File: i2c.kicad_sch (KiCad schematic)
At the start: 2 parts, among them U1 74HC237, U2 74HC237

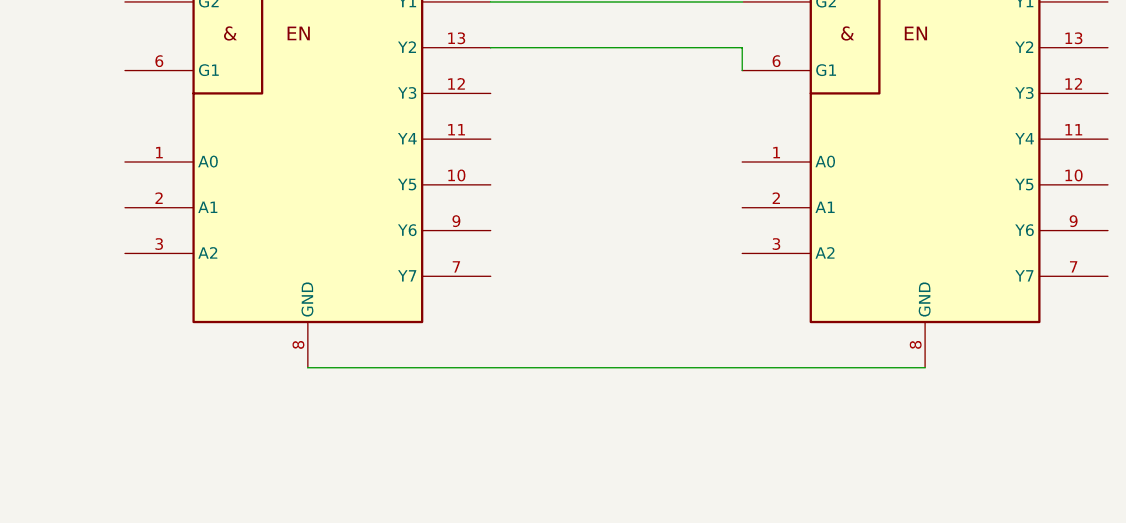
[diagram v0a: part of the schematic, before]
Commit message: se agregaron nuevas lineas de comunicacion
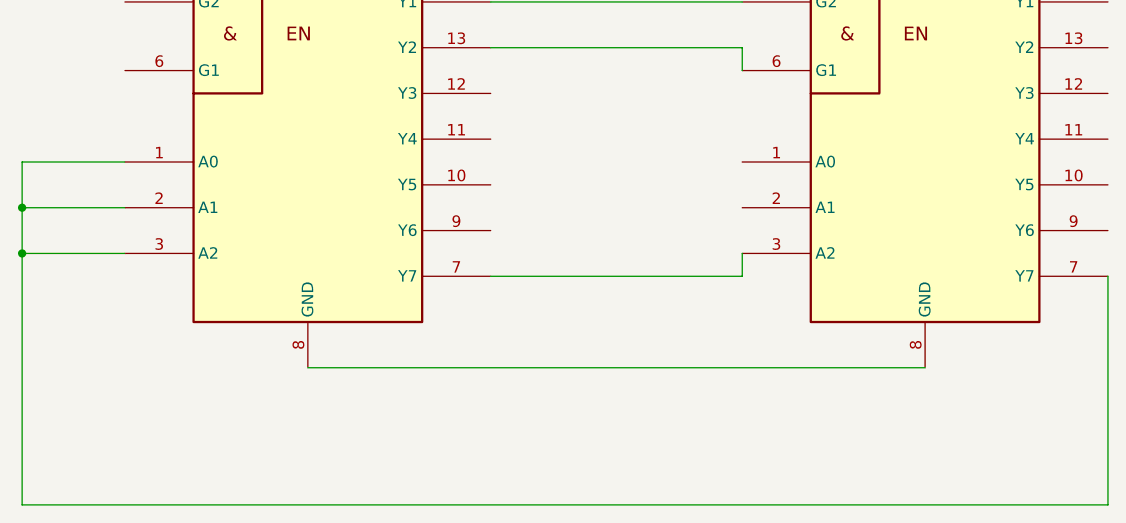
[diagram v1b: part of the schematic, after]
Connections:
- net at U2.3 (A2): now also U1.7 (Y7)
- net at U2.7 (Y7): now also U1.1 (A0), U1.2 (A1), U1.3 (A2)
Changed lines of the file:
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@@
 	(generator_version "9.0")
 	(paper "A4")
+	(junction
+		(at 53.34 71.12)
+		(diameter 0)
+		(color 0 0 0 0)
+	)
+	(junction
+		(at 53.34 76.2)
+		(diameter 0)
+		(color 0 0 0 0)
+	)
+	(wire
+		(pts
+			(xy 53.34 76.2) (xy 53.34 71.12)
+		)
+		(stroke
+			(width 0)
+			(type default)
+		)
+	)
 	(wire
 		(pts
 			(xy 105.41 53.34) (xy 133.35 53.34)
+		)
+		(stroke
+			(width 0)
+			(type default)
+		)
+	)
+	(wire
+		(pts
+			(xy 53.34 66.04) (xy 64.77 66.04)
+		)
+		(stroke
+			(width 0)
+			(type default)
+		)
+	)
+	(wire
+		(pts
+			(xy 133.35 78.74) (xy 133.35 76.2)
+		)
+		(stroke
+			(width 0)
+			(type default)
+		)
+	)
+	(wire
+		(pts
+			(xy 173.99 78.74) (xy 173.99 104.14)
 		)
 		(stroke
@@
 	(wire
 		(pts
+			(xy 105.41 78.74) (xy 133.35 78.74)
+		)
+		(stroke
+			(width 0)
+			(type default)
+		)
+	)
+	(wire
+		(pts
+			(xy 173.99 104.14) (xy 53.34 104.14)
+		)
+		(stroke
+			(width 0)
+			(type default)
+		)
+	)
+	(wire
+		(pts
 			(xy 105.41 48.26) (xy 133.35 48.26)
 		)
 		(stroke
+			(width 0)
+			(type default)
+		)
+	)
+	(wire
+		(pts
+			(xy 53.34 76.2) (xy 64.77 76.2)
+		)
+		(stroke
+			(width 0)
+			(type default)
+		)
+	)
+	(wire
+		(pts
+			(xy 53.34 71.12) (xy 53.34 66.04)
+		)
+		(stroke
+			(width 0)
+			(type default)
+		)
+	)
+	(wire
+		(pts
+			(xy 53.34 104.14) (xy 53.34 76.2)
+		)
+		(stroke
+			(width 0)
+			(type default)
+		)
+	)
+	(wire
+		(pts
+			(xy 53.34 71.12) (xy 64.77 71.12)
+		)
+		(stroke

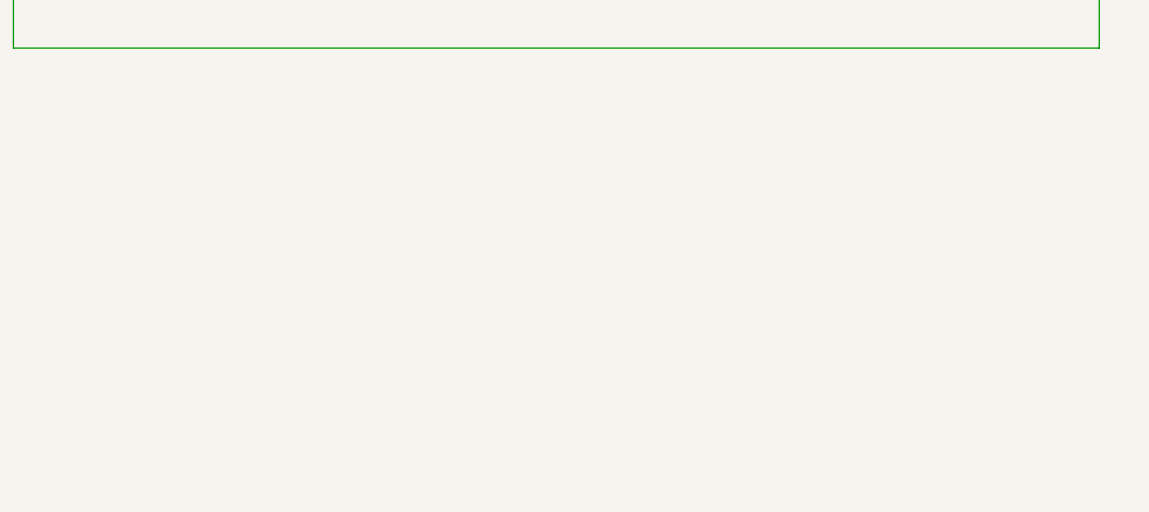
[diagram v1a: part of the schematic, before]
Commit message: se agregaron 2 componentes nuevos
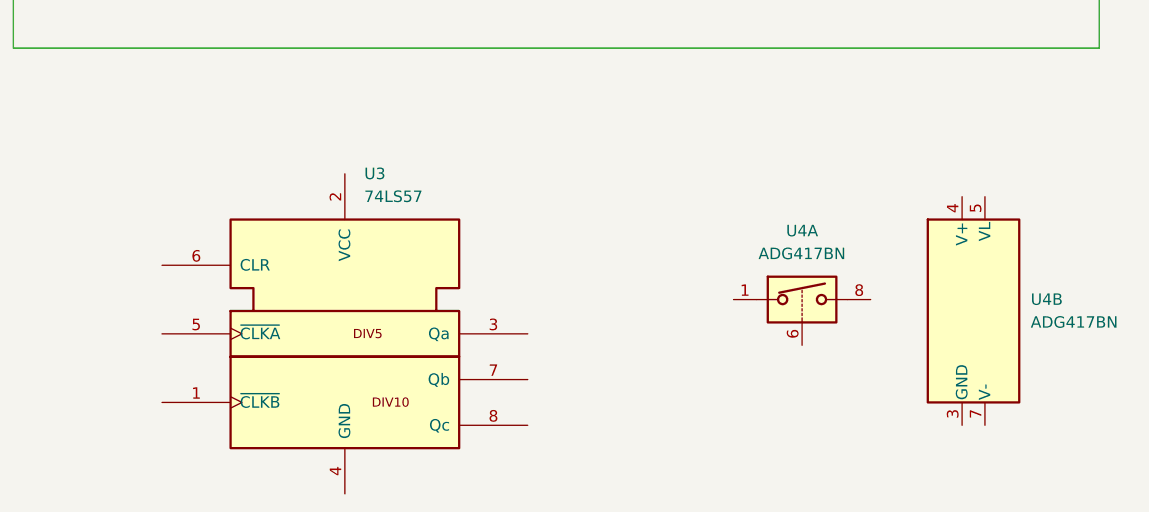
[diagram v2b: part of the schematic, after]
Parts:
- added U3: 74LS57, symbol 74xx_IEEE:74LS57
- added U4: ADG417BN, Package_DIP:DIP-8_W7.62mm, symbol Analog_Switch:ADG417BN
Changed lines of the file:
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@@
+	)
+	(symbol
+		(lib_id "Analog_Switch:ADG417BN")
+		(at 158.75 133.35 0)
+		(unit 2)
+		(exclude_from_sim no)
+		(in_bom yes)
+		(on_board yes)
+		(dnp no)
+		(fields_autoplaced yes)
+		(property "Reference" "U4"
+			(at 166.37 132.0799 0)
+			(effects
+				(font
+					(size 1.27 1.27)
+				)
+				(justify left)
+			)
+		)
+		(property "Value" "ADG417BN"
+			(at 166.37 134.6199 0)
+			(effects
+				(font
+					(size 1.27 1.27)
+				)
+				(justify left)
+			)
+		)
+		(property "Footprint" "Package_DIP:DIP-8_W7.62mm"
+			(at 158.75 135.89 0)
+			(effects
+				(font
+					(size 1.27 1.27)
+				)
+				(hide yes)
+			)
+		)
+		(property "Datasheet" "https://www.analog.com/media/en/technical-documentation/data-sheets/ADG417.pdf"
+			(at 158.75 133.35 0)
+			(effects
+				(font
+					(size 1.27 1.27)
+				)
+				(hide yes)
+			)
+		)
+		(property "Description" "Single SPST Monolithic LC²MOS Analog Switch, normally OFF, 25Ohm Ron, DIP-8"
+			(at 158.75 133.35 0)
+			(effects
+				(font
+					(size 1.27 1.27)
+				)
+				(hide yes)
+			)
+		)
+		(pin "5"
+		)
+		(pin "2"
+		)
+		(pin "3"
+		)
+		(pin "6"
+		)
+		(pin "8"
+		)
+		(pin "1"
+		)
+		(pin "4"
+		)
+		(pin "7"
+		)
+		(instances
+			(project ""
+				(path "/5d2edb2c-ac7e-435f-ae04-6809c3a8fc26"
+					(reference "U4")
+					(unit 2)
+				)
+			)
+		)
+	)
+	(symbol
+		(lib_id "Analog_Switch:ADG417BN")
+		(at 140.97 132.08 0)
+		(unit 1)
+		(exclude_from_sim no)
+		(in_bom yes)
+		(on_board yes)
+		(dnp no)
+		(fields_autoplaced yes)
+		(property "Reference" "U4"
+			(at 140.97 124.46 0)
+			(effects
+				(font
+					(size 1.27 1.27)
+				)
+			)
+		)
+		(property "Value" "ADG417BN"
+			(at 140.97 127 0)
+			(effects
+				(font
+					(size 1.27 1.27)
+				)
+			)
+		)
+		(property "Footprint" "Package_DIP:DIP-8_W7.62mm"
+			(at 140.97 134.62 0)
+			(effects
+				(font
+					(size 1.27 1.27)
+				)
+				(hide yes)
+			)
+		)
+		(property "Datasheet" "https://www.analog.com/media/en/technical-documentation/data-sheets/ADG417.pdf"
+			(at 140.97 132.08 0)
+			(effects
+				(font
+					(size 1.27 1.27)
+				)
+				(hide yes)
+			)
+		)
+		(property "Description" "Single SPST Monolithic LC²MOS Analog Switch, normally OFF, 25Ohm Ron, DIP-8"
+			(at 140.97 132.08 0)
+			(effects
+				(font
+					(size 1.27 1.27)
+				)
+				(hide yes)
+			)
+		)
+		(pin "5"
+		)
+		(pin "2"
+		)
+		(pin "3"
+		)
+		(pin "6"
+		)
+		(pin "8"
+		)
+		(pin "1"
+		)
+		(pin "4"
+		)
+		(pin "7"
+		)
+		(instances
+			(project ""
+				(path "/5d2edb2c-ac7e-435f-ae04-6809c3a8fc26"
+					(reference "U4")
+					(unit 1)
+				)
+			)
+		)
+	)
+	(symbol
+		(lib_id "74xx_IEEE:74LS57")
+		(at 90.17 135.89 0)
+		(unit 1)
+		(exclude_from_sim no)
+		(in_bom yes)
+		(on_board yes)
+		(dnp no)
+		(fields_autoplaced yes)
+		(property "Reference" "U3"
+			(at 92.3133 118.11 0)
+			(effects
+				(font
+					(size 1.27 1.27)
+				)
+				(justify left)
+			)
+		)
+		(property "Value" "74LS57"
+			(at 92.3133 120.65 0)
+			(effects
+				(font
+					(size 1.27 1.27)
+				)
+				(justify left)
+			)
+		)
+		(property "Footprint" ""
+			(at 90.17 135.89 0)
+			(effects
+				(font
+					(size 1.27 1.27)
+				)
+				(hide yes)
+			)
+		)
+		(property "Datasheet" ""
+			(at 90.17 135.89 0)
+			(effects
+				(font
+					(size 1.27 1.27)
+				)
+				(hide yes)
+			)
+		)
+		(property "Description" ""
+			(at 90.17 135.89 0)
+			(effects
+				(font
+					(size 1.27 1.27)
+				)
+				(hide yes)
+			)
+		)
+		(pin "2"
+		)
+		(pin "6"
+		)
+		(pin "3"
+		)
+		(pin "7"
+		)
+		(pin "5"
+		)
+		(pin "1"
+		)
+		(pin "8"
+		)
+		(pin "4"
+		)
+		(instances
+			(project ""
+				(path "/5d2edb2c-ac7e-435f-ae04-6809c3a8fc26"
+					(reference "U3")
+					(unit 1)
+				)
+			)
+		)
 	)
 	(symbol

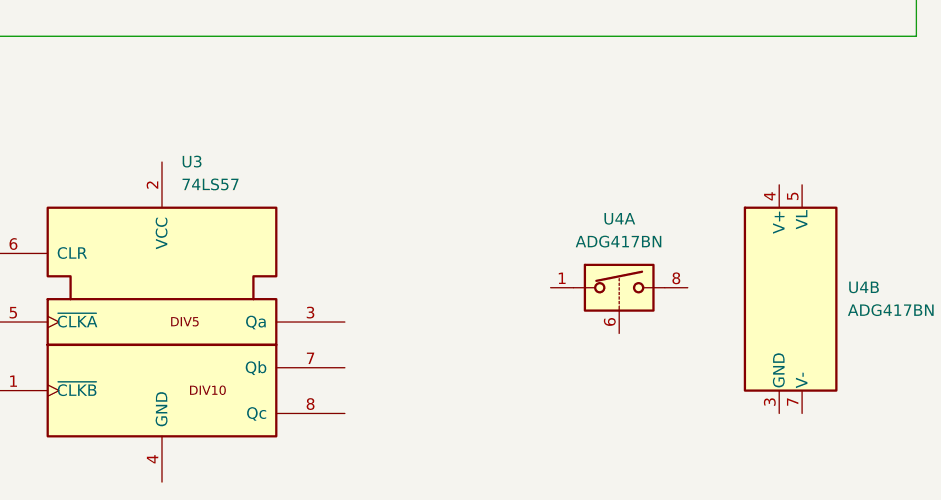
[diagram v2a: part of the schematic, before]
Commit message: se agregaron 2 componenetes nuevos y se ajusto el pcb, falta agregar footprints
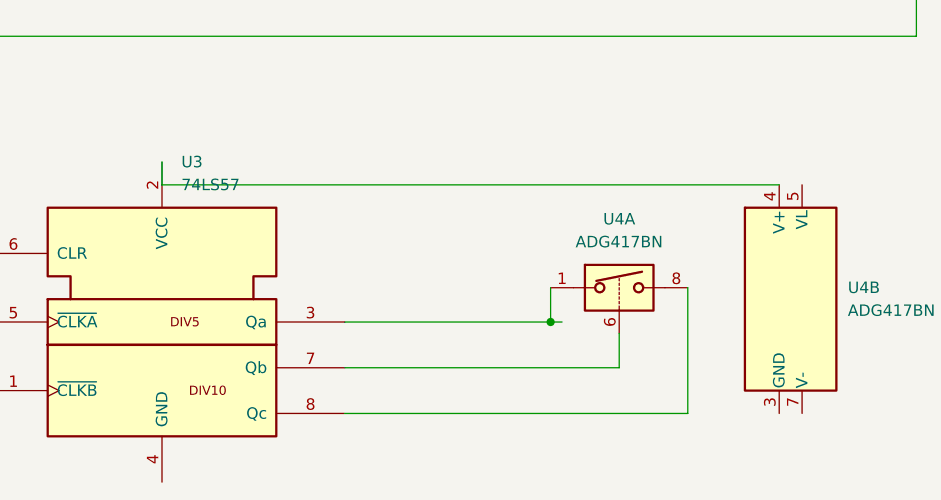
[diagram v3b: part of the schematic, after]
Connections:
- net at U4.4 (V+): now also U3.2 (VCC)
- net at U4.1: now also U3.3 (Qa)
- net at U4.6: now also U3.7 (Qb)
- net at U4.8: now also U3.8 (Qc)
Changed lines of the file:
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@@
+		(color 0 0 0 0)
+	)
+	(junction
+		(at 133.35 135.89)
+		(diameter 0)
 		(color 0 0 0 0)
 	)
@@
 	(wire
 		(pts
+			(xy 133.35 135.89) (xy 133.35 132.08)
+		)
+		(stroke
+			(width 0)
+			(type default)
+		)
+	)
+	(wire
+		(pts
+			(xy 140.97 140.97) (xy 140.97 137.16)
+		)
+		(stroke
+			(width 0)
+			(type default)
+		)
+	)
+	(wire
+		(pts
+			(xy 110.49 146.05) (xy 148.59 146.05)
+		)
+		(stroke
+			(width 0)
+			(type default)
+		)
+	)
+	(wire
+		(pts
+			(xy 158.75 120.65) (xy 90.17 120.65)
+		)
+		(stroke
+			(width 0)
+			(type default)
+		)
+	)
+	(wire
+		(pts
+			(xy 133.35 135.89) (xy 134.62 135.89)
+		)
+		(stroke
+			(width 0)
+			(type default)
+		)
+	)
+	(wire
+		(pts
 			(xy 53.34 76.2) (xy 64.77 76.2)
 		)
 		(stroke
+			(width 0)
+			(type default)
+		)
+	)
+	(wire
+		(pts
+			(xy 110.49 140.97) (xy 140.97 140.97)
+		)
+		(stroke
+			(width 0)
+			(type default)
+		)
+	)
+	(wire
+		(pts
+			(xy 148.59 146.05) (xy 148.59 132.08)
+		)
+		(stroke
+			(width 0)
+			(type default)
+		)
+	)
+	(wire
+		(pts
+			(xy 90.17 120.65) (xy 90.17 118.11)
+		)
+		(stroke
+			(width 0)
+			(type default)
+		)
+	)
+	(wire
+		(pts
+			(xy 110.49 135.89) (xy 133.35 135.89)
+		)
+		(stroke
